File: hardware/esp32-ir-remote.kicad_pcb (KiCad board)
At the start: 2 copper layers, 92 x 44 mm, 56 parts, among them J2 USB_C_Receptacle_USB2.0_14P, J4 GPIO_PWR, J5 EXT_IR, Q3 AO3400A, SW1 RESET, SW2 BOOT, U1 AMS1117-3.3, U3 ESP32-C3-WROOM-02, U4 TSOP382xx, U5 AHT20

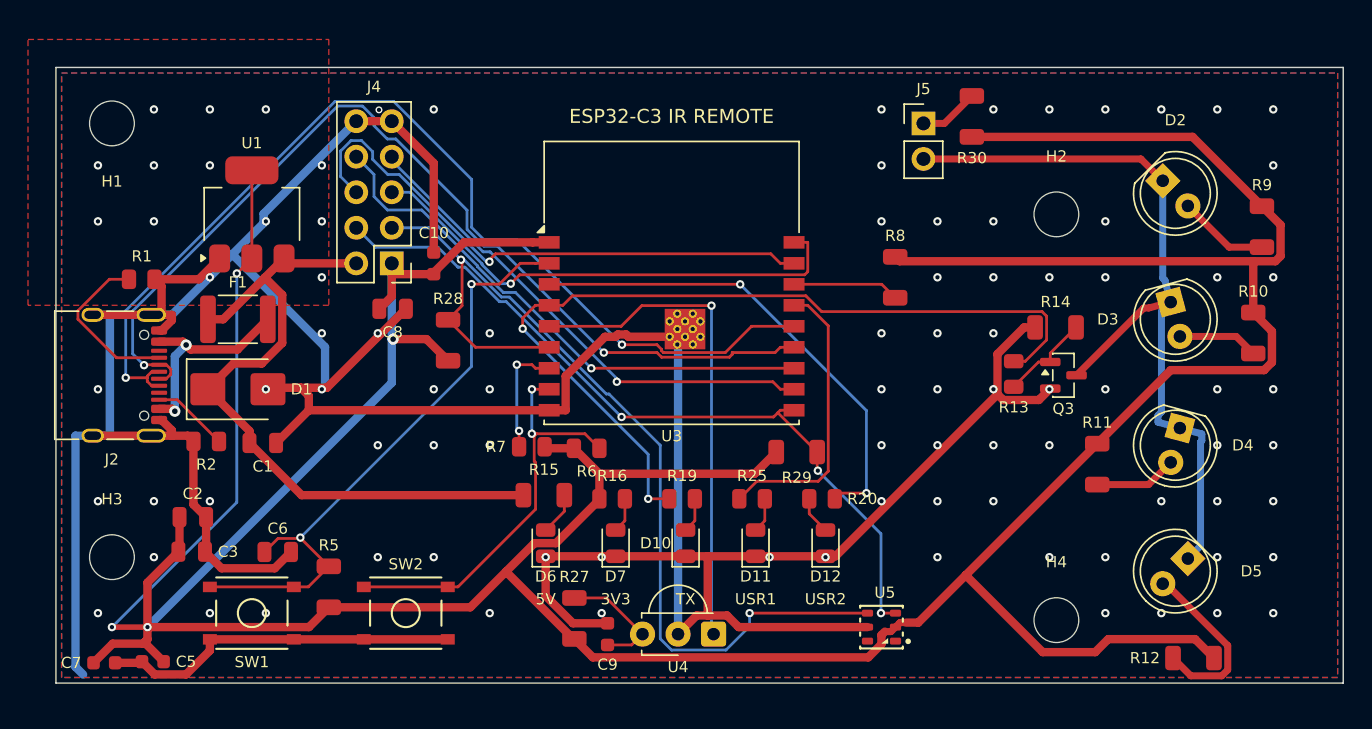
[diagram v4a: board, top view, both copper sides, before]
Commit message: hw(pcb): Phase B decoupling re-seat + full re-route; Power min-width DRU
Fix the "decoupling far from pins" MOD finding. pcb_place_v2.py's net
heuristic can't distribute a shared rail: a +3.3V bypass cap pad sees the
whole net, so it seated at the nearest rail pin, piling every MCU/sensor
bypass onto the LDO and leaving U5 (AHT20) with no local cap (two 10uF
stacked on U3, both 100nF orphaned ~50mm away).

pcb_place_v2.py: add an explicit ASSIGN map pinning each bypass / EN-RC /
I2C-pullup to the specific (anchor, pad) it serves, so every IC gets its
own HF+bulk bank:
  U3  <- C7 100nF + C8 10uF on 3V3 (~7-8mm, module-courtyard bound);
         C6 1uF EN power-on-reset RC on EN
  U5  <- C5 100nF + C10 10uF on VDD + R28/R29 I2C pull-ups (~2-4mm) --
         U5 went from bare to a full local bank
  U1  <- C1 in-cap on VIN, C2/C3 out-caps on VOUT
Refs not listed keep the net heuristic (R27/C9 uniquely reach U4).

Re-route: rip -> FreeRouting (0 unrouted) -> GND + LDO pour -> silk.
DRC 0 errors / 0 unconnected / 0 parity; hardware_validate.py EXIT 0
(schematic untouched -> netlist electrically identical).

Power width + DRU (brief item 1): the new route holds the 0.6mm Power
class (old 0.2mm +3.3V segments gone; min 0.50mm at a few pad necks), so
add the previously-deferred Power min-width DRU (0.5mm) to the .kicad_dru.

Cosmetic: +1 silk_over_copper in the denser SE sensor corner (ref over a
track) -- accepted tradeoff for U5's local decoupling; baseline refresh
follows.
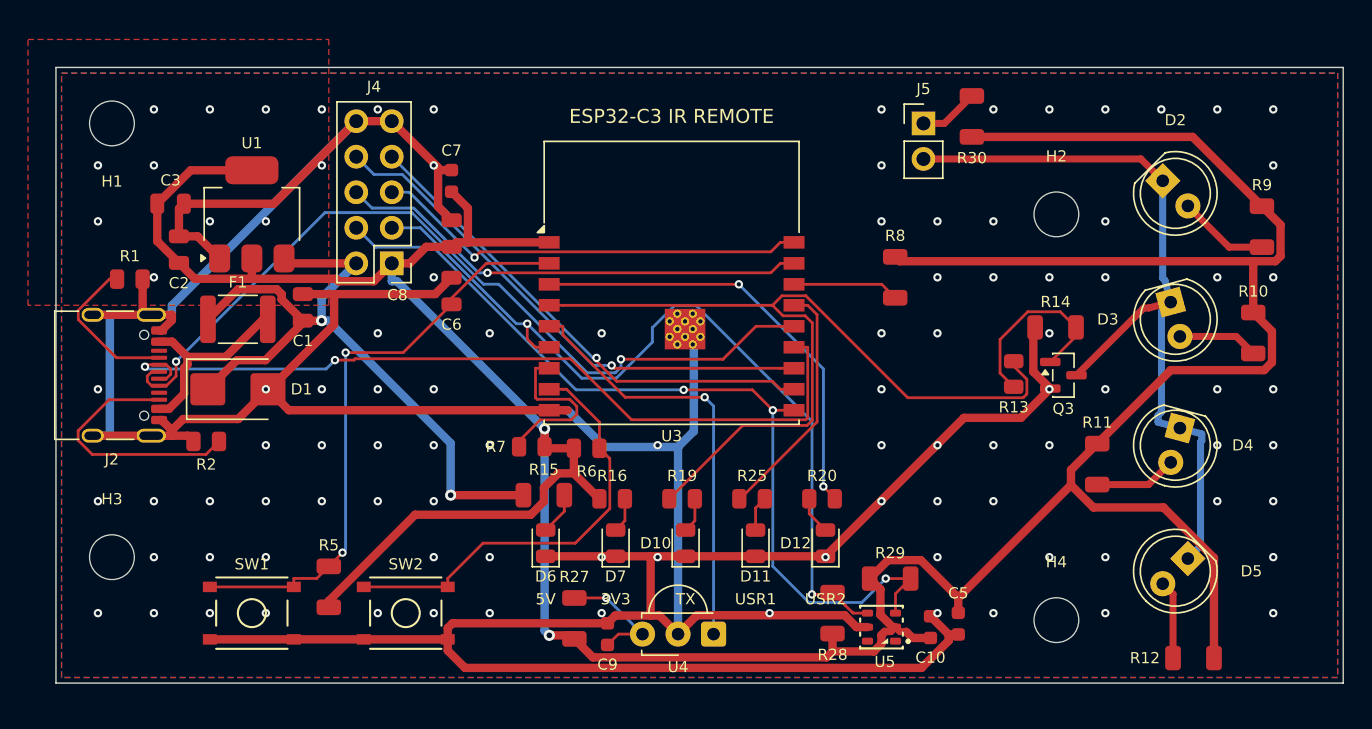
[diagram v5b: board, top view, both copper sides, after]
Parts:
- moved C5 57.6 mm to (170.5, 109.8), turned to 90 degrees
- moved C10 44.0 mm to (168.5, 110.0)
- moved C7 42.4 mm to (134.3, 78.1), turned to 90 degrees
- moved R28 33.7 mm to (161.5, 109.0)
- moved C3 24.9 mm to (114.2, 79.7)
- moved C6 22.4 mm to (134.3, 86.0), turned to 90 degrees
- moved C2 19.1 mm to (114.8, 83.0), turned to 90 degrees
- moved R29 11.2 mm to (165.6, 106.5)
- moved C1 10.1 mm to (123.7, 87.2), turned to 90 degrees
- moved C8 6.84 mm to (134.3, 81.9), turned to 90 degrees
- moved R1 0.85 mm to (111.3, 85.1)
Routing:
- net +3.3V: track 315.1 -> 264.1 mm, vias 4 -> 2
- net GND: track 292.2 -> 313.6 mm, vias 91 -> 99
- net /USB_D+: track 72.9 -> 59.9 mm
- net Net-(J2-CC2): track 5.52 -> 18.3 mm
- net /USB_D-: track 69.9 -> 59.0 mm
- net /I2C_SDA: track 69.2 -> 60.6 mm
- net Net-(D5-A): track 12.8 -> 5.62 mm
- net Net-(Q3-G): track 6.58 -> 13.7 mm
- net /I2C_SCL: track 55.5 -> 62.4 mm
- net /SPARE_IO1: track 40.6 -> 34.0 mm
- net /IR_RX: track 35.8 -> 30.8 mm
- net /SPARE_IO0: track 35.9 -> 31.1 mm
- net /IO8_STRAP: track 8.35 -> 12.2 mm, vias 2 -> 0
- net /USER_LED1: track 20.6 -> 17.4 mm
- net /USER_LED2: track 34.7 -> 31.7 mm
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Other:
- board text added: "2026-06-15 git 42998de-dirty"
- board text removed: "2026-06-15 git 92c3a90-dirty"

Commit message: hw(autoresearch): run GPIO remap as its own subprocess (SWIG-safe)
In-process gr.apply() after the floorplan's repeated Load/Save corrupted the
SWIG board state. Run it as a clean subprocess like every other stage.

Demonstrated: remapping USER_LED2 off the far-W S-row pad to a N-row pad near
its LED resistor routes it (Layout B 5->4 unrouted) AND freed congestion so the
router put USB D+/D- fully on F.Cu (0 B.Cu, 0 vias) -- the SI win. Remaining 4
unrouted are the USB-C connector overhanging the N edge (GND shield + VBUS).
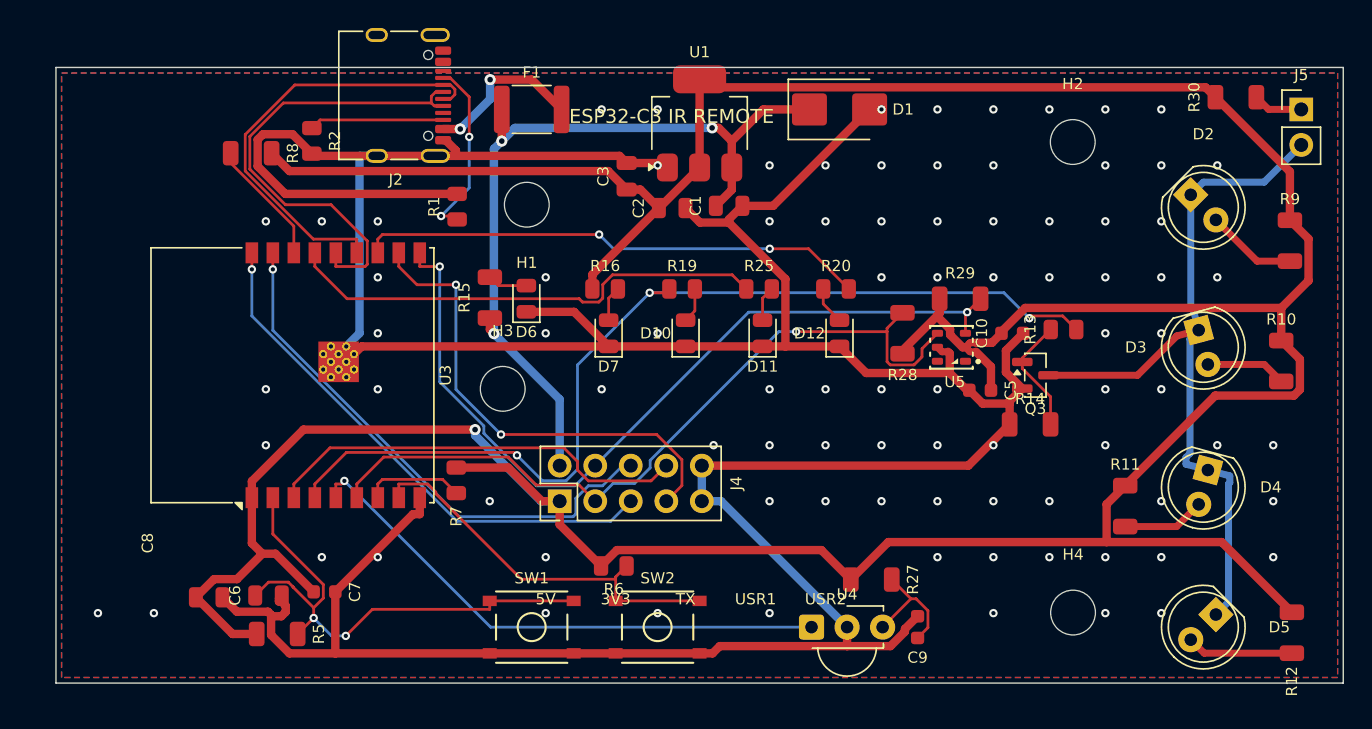
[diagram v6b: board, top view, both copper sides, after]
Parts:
- moved D1 47.4 mm to (162.0, 73.0)
- moved R8 46.9 mm to (120.0, 76.1), turned to 0 degrees
- moved C2 35.4 mm to (150.0, 80.0), turned to 0 degrees
- moved C3 32.7 mm to (146.8, 77.8), turned to 90 degrees
- moved U1 32.7 mm to (152.0, 74.0)
- moved C1 31.3 mm to (154.1, 79.9), turned to 0 degrees
- moved C8 31.2 mm to (117.0, 107.9), turned to 0 degrees
- moved C7 30.7 mm to (125.2, 107.5), turned to 0 degrees
- moved H3 30.4 mm to (137.9, 93.0)
- moved H1 30.2 mm to (139.7, 79.8)
- moved J2 28.5 mm to (130.0, 72.0)
- moved J5 27.0 mm to (195.0, 73.0)
- moved F1 25.8 mm to (140.0, 73.0)
- moved C6 25.4 mm to (121.2, 107.7), turned to 0 degrees
- moved U3 24.3 mm to (126.0, 92.0), turned to 90 degrees
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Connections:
- U3 pad 12: /SPARE_TX -> /USER_LED2
- U3 pad 3: /USER_LED2 -> /SPARE_TX
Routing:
- net GND: track 313.6 -> 278.0 mm, vias 99 -> 87
- net /USB_D-: track 59.0 -> 31.5 mm, vias 2 -> 0
- net /USB_D+: track 59.9 -> 34.2 mm, vias 2 -> 0
- net +3.3V: track 264.1 -> 281.4 mm, vias 2 -> 1
- net /USER_LED1: track 17.4 -> 34.7 mm
- net Net-(J2-CC2): track 18.3 -> 9.62 mm
- net /IR_RX: track 30.8 -> 39.4 mm
- net /SPARE_IO0: track 31.1 -> 38.3 mm
- net /SPARE_TX: track 37.6 -> 30.5 mm, vias 1 -> 0
- net /IR_TX: track 63.2 -> 69.9 mm, vias 0 -> 3
- net +5V: track 51.3 -> 57.7 mm, vias 2 -> 3
- net /I2C_SDA: track 60.6 -> 55.2 mm, vias 2 -> 1
- net Net-(Q3-G): track 13.7 -> 8.46 mm
- net /IO8_STRAP: track 12.2 -> 7.13 mm
- net /SPARE_IO1: track 34.0 -> 38.8 mm
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- removed copper zone on F.Cu, net +3.3V

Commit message: hw: Layout B routes 0/0 on 2 layers — LDO thermal pour + USB mouth-N
The autoresearch loop closed Layout B (U3 rot90, antenna W) to 0 DRC / 0
unrouted on 2 layers — the open question from the rotation thread.

Floorplan (pcb_floorplan.ANCHORS):
- U1 (LDO) in the open NE -> 433mm2 +3.3V tab thermal pour (Nick's big-pour
  ask). pcb_ldo_pour now tracks U1's tab to the nearest edge (was hardcoded
  NW) and the pour area is scored (pcb_score).
- J2 USB-C rot180 so the receptacle MOUTH faces N off the board edge (rot90/
  270 faced sideways, unusable). Shallower (4.7mm) -> pads on-board, mouth
  overhangs.
- U5 (AHT20) relocated ~38mm from the LDO (sensor accuracy).
- F1/D1 spread along the N edge; no power-corner cram.

Harness: pcb_experiment runs pcb_ldo_pour + scores pour area; --anchors
override; _legalize_flex honours overridden FLEX targets; GPIO remap as its
own SWIG-safe subprocess.

Board routes 0/0 WITHOUT the GPIO remap, so it stays schematic-parity-valid
(netlist untouched). USB on B.Cu (2-4 vias, full-speed-fine, as shipping).
Remaining: optional USB->F.Cu, USB-C 3D reseat at rot180, CI baseline refresh.
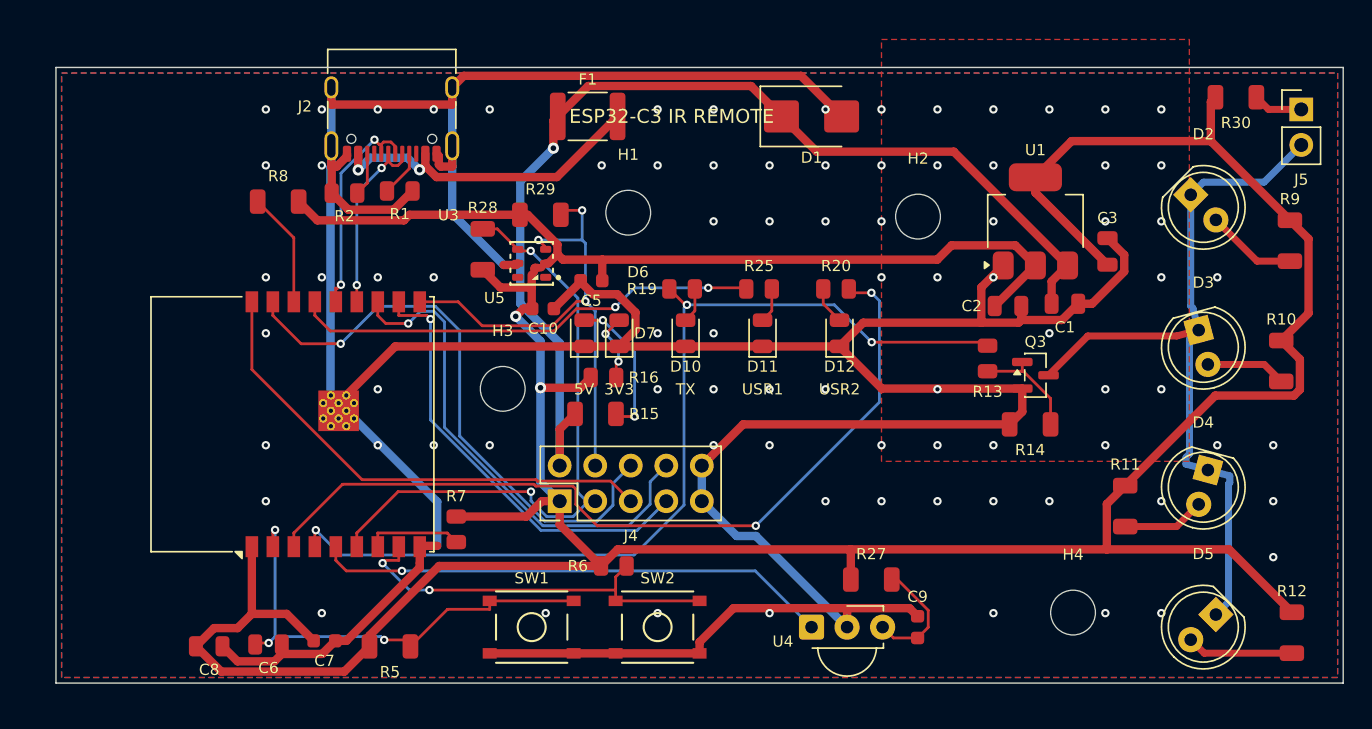
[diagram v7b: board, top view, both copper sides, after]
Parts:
- moved C3 34.8 mm to (181.2, 83.2)
- moved C10 33.6 mm to (140.8, 87.2)
- moved R28 30.6 mm to (136.5, 83.0)
- moved R29 30.6 mm to (140.6, 80.5)
- moved U5 30.6 mm to (140.0, 84.0)
- moved C5 28.9 mm to (144.3, 85.2)
- moved C1 25.0 mm to (178.1, 86.9)
- moved C2 25.0 mm to (174.0, 87.0)
- moved U1 25.0 mm to (176.0, 81.0)
- moved H2 12.3 mm to (167.6, 80.7)
- moved R15 11.2 mm to (144.6, 94.8), turned to 0 degrees
- moved R5 8.11 mm to (129.9, 111.4)
- moved H1 7.27 mm to (146.9, 80.4)
- moved R16 6.33 mm to (145.1, 92.2)
- moved R13 5.81 mm to (172.6, 90.8), turned to 90 degrees
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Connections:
- U3 pad 12: /USER_LED2 -> /SPARE_TX
- U3 pad 3: /SPARE_TX -> /USER_LED2
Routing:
- net GND: track 278.0 -> 303.6 mm, vias 87 -> 82
- net /USER_LED2: track 36.4 -> 59.6 mm
- net /I2C_SCL: track 59.8 -> 37.6 mm, vias 2 -> 3
- net +5V: track 57.7 -> 77.3 mm, vias 3 -> 1
- net /USB_D+: track 34.2 -> 15.8 mm, vias 0 -> 2
- net /USB_D-: track 31.5 -> 13.3 mm, vias 0 -> 2
- net Net-(F1-Pad2): track 11.6 -> 23.5 mm
- net /I2C_SDA: track 55.2 -> 44.5 mm, vias 1 -> 2
- net Net-(J2-CC1): track 13.0 -> 3.32 mm, vias 2 -> 0
- net Net-(D6-A): track 2.86 -> 10.6 mm, vias 0 -> 2
- net +3.3V: track 281.4 -> 274.2 mm, vias 1 -> 2
- net Net-(J2-CC2): track 9.62 -> 3.11 mm
- net /SPARE_TX: track 30.5 -> 35.7 mm, vias 0 -> 1
- net /ESP_EN: track 37.8 -> 33.9 mm, vias 2 -> 3
- net /SPARE_RX: track 34.7 -> 31.5 mm, vias 2 -> 1
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- added copper zone on F.Cu, net +3.3V
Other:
- board text added: "2026-06-16 git 3b077d0-dirty"
- board text removed: "2026-06-15 git 42998de-dirty"
